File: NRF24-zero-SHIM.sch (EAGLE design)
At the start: 33 parts

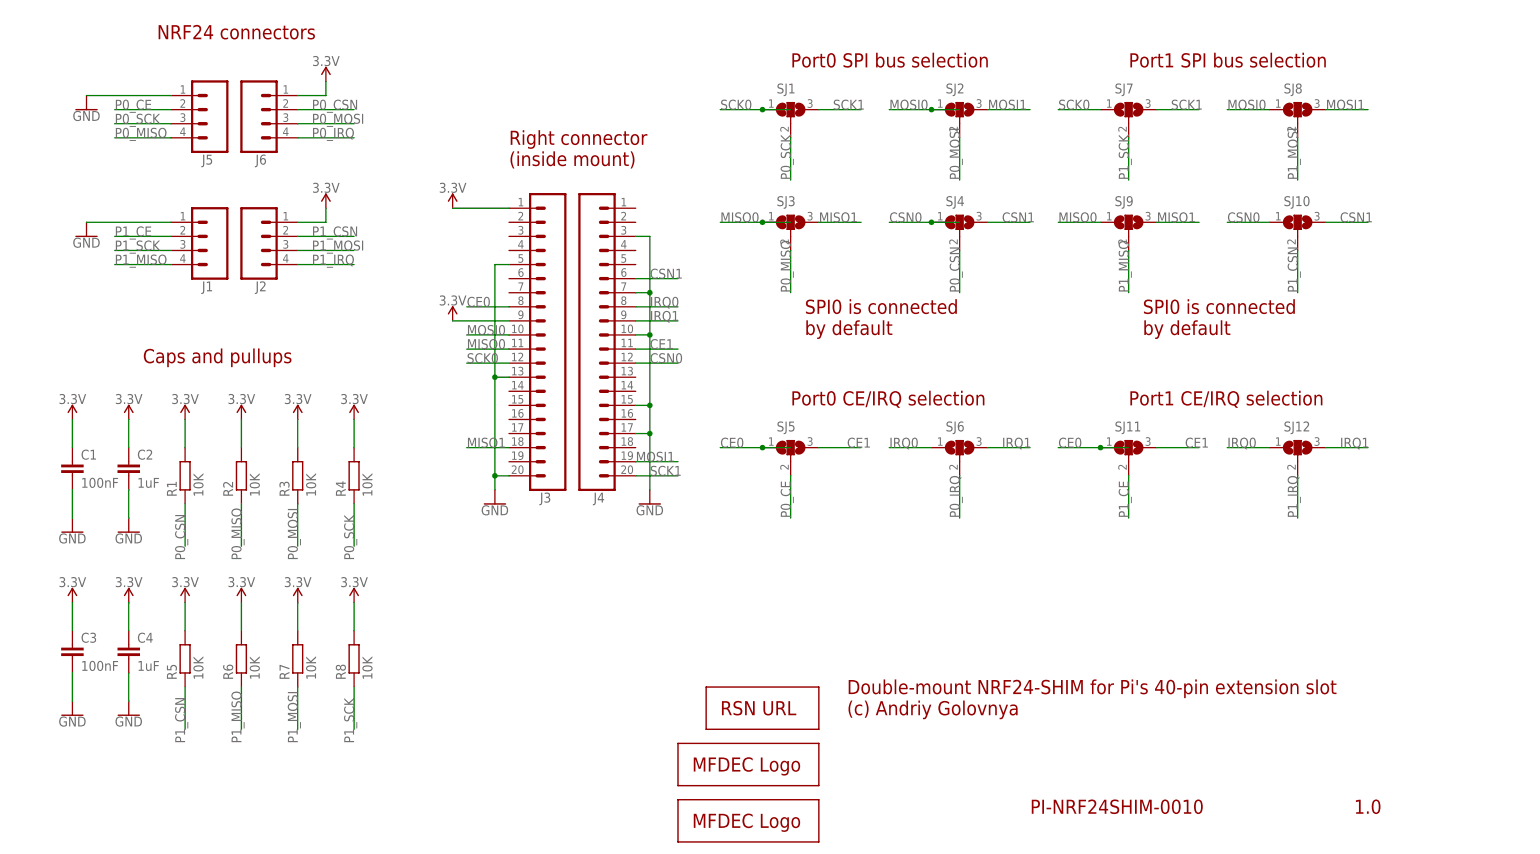
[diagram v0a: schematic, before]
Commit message: Changed the way how solder joins are organized.
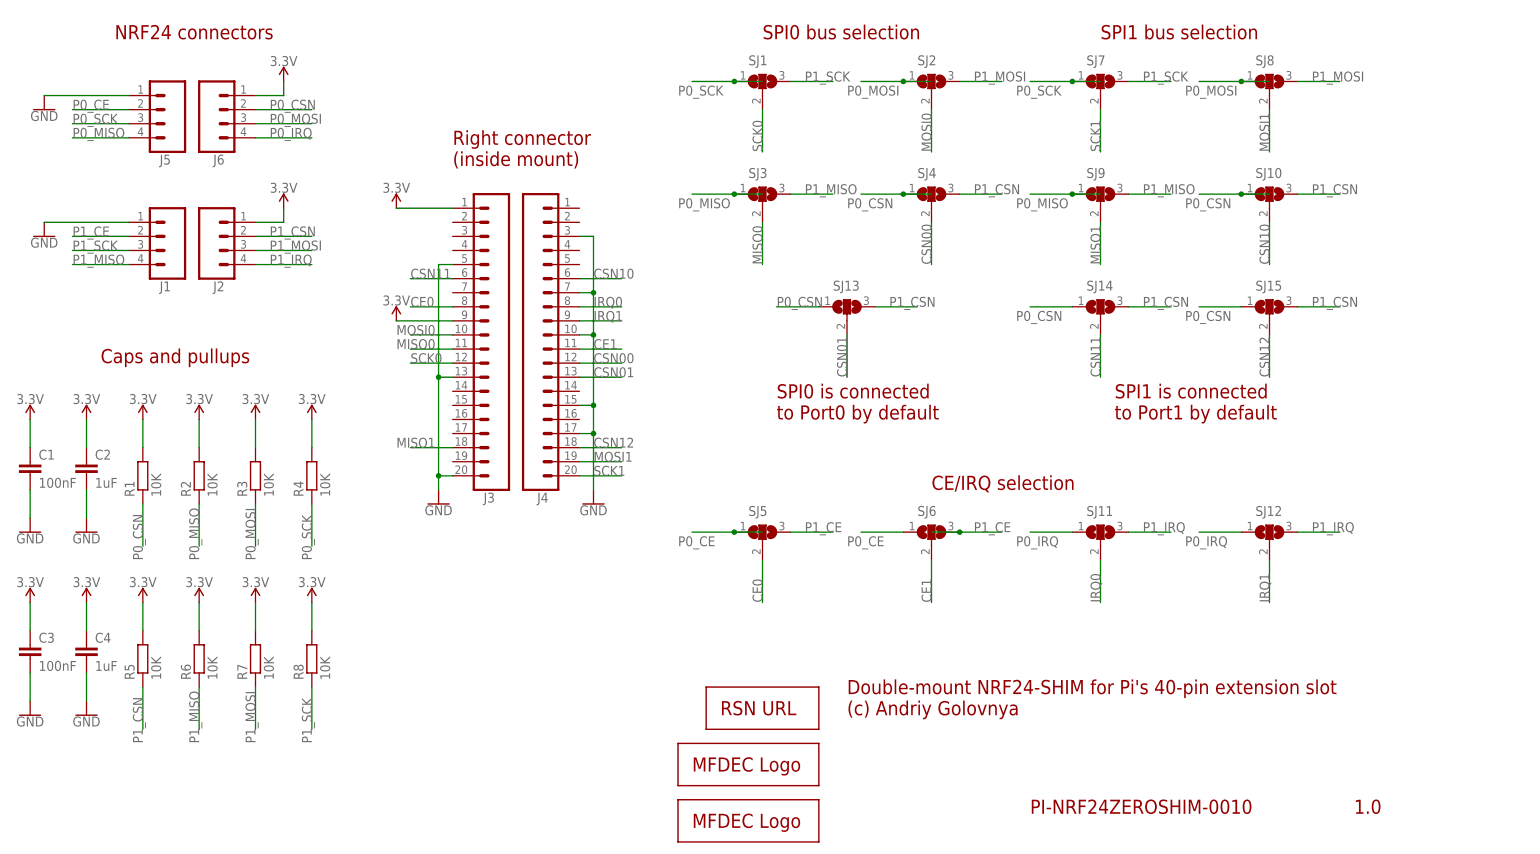
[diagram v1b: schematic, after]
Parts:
- added SJ13, SJ14, SJ15: (no value), _my_jumpers:SJ2
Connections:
- removed net CSN0: J4.12, SJ10.1, SJ4.1
- removed net CSN1: J4.6, SJ10.3, SJ4.3
- new net CSN00: J4.12, SJ4.2
- new net CSN01: J4.13, SJ13.2
- new net CSN10: J4.6, SJ10.2
- new net CSN11: J3.6, SJ14.2
- new net CSN12: J4.18, SJ15.2
- net CE0: now also SJ5.2; no longer SJ11.1, SJ5.1
- net CE1: now also SJ6.2; no longer SJ11.3, SJ5.3
- net IRQ0: now also SJ11.2; no longer SJ12.1, SJ6.1
- net IRQ1: now also SJ12.2; no longer SJ12.3, SJ6.3
- net MISO0: now also SJ3.2; no longer SJ3.1, SJ9.1
- net MISO1: now also SJ9.2; no longer SJ3.3, SJ9.3
- net MOSI0: now also SJ2.2; no longer SJ2.1, SJ8.1
- net MOSI1: now also SJ8.2; no longer SJ2.3, SJ8.3
- net P0_CE: now also SJ5.1, SJ6.1; no longer SJ5.2
- net P0_CSN: now also SJ10.1, SJ13.1, SJ14.1, SJ15.1, SJ4.1; no longer SJ4.2
- net P0_IRQ: now also SJ11.1, SJ12.1; no longer SJ6.2
- net P0_MISO: now also SJ3.1, SJ9.1; no longer SJ3.2
- net P0_MOSI: now also SJ2.1, SJ8.1; no longer SJ2.2
- net P0_SCK: now also SJ1.1, SJ7.1; no longer SJ1.2
- net P1_CE: now also SJ5.3, SJ6.3; no longer SJ11.2
- net P1_CSN: now also SJ10.3, SJ13.3, SJ14.3, SJ15.3, SJ4.3; no longer SJ10.2
- net P1_IRQ: now also SJ11.3, SJ12.3; no longer SJ12.2
- net P1_MISO: now also SJ3.3, SJ9.3; no longer SJ9.2
- net P1_MOSI: now also SJ2.3, SJ8.3; no longer SJ8.2
- net P1_SCK: now also SJ1.3, SJ7.3; no longer SJ7.2
- net SCK0: now also SJ1.2; no longer SJ1.1, SJ7.1
- net SCK1: now also SJ7.2; no longer SJ1.3, SJ7.3
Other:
- note added: "CE/IRQ selection"
- note added: "PI-NRF24ZEROSHIM-0010"
- note added: "SPI0 bus selection"
- note added: "SPI0 is connected to Port0 by default"
- note added: "SPI1 bus selection"
- note added: "SPI1 is connected to Port1 by default"
- note removed: "PI-NRF24SHIM-0010"
- note removed: "Port0 CE/IRQ selection"
- note removed: "Port0 SPI bus selection"
- note removed: "Port1 CE/IRQ selection"
- note removed: "Port1 SPI bus selection"
- note removed: "SPI0 is connected by default"
- moved on the sheet: C1, C2, C3, C4, J1, J2, J3, J4, J5, J6, R1, R2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

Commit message: Added zero-sized board.
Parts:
- removed LOGO2: MFDECLOGO_L_20MM, _my_logos:MFDECLOGO_L_20MM
- added SJ16: (no value), _my_jumpers:SJ2
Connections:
- new net CE2: J3.7, SJ6.2
- net CE0: now also SJ16.2; no longer SJ5.2
- net CE1: now also SJ5.2; no longer SJ6.2
- net P0_CE: now also SJ16.1
- net P1_CE: now also SJ16.3
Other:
- moved on the sheet: J3, J4

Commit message: Simplified document names. Generated PDF schematics.
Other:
- note added: "PI-NRF24ZS-0010"
- note removed: "PI-NRF24ZEROSHIM-0010"
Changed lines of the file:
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@@
 <plain>
 <text x="256.54" y="7.62" size="2.54" layer="94">1.0</text>
-<text x="198.12" y="7.62" size="2.54" layer="94">PI-NRF24ZEROSHIM-0010</text>
+<text x="198.12" y="7.62" size="2.54" layer="94">PI-NRF24ZS-0010</text>
 <text x="165.1" y="25.4" size="2.54" layer="94">Double-mount NRF24-SHIM for Pi's 40-pin extension slot
 (c) Andriy Golovnya</text>
